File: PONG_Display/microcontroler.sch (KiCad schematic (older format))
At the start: 16 parts

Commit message: V3
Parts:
- added BT?: Battery_Cell, symbol Device:Battery_Cell
- added C? (x2): 22p, symbol Device:C
- added C? (x6): 100n, symbol Device:C
- added R? (x2): 10k, symbol Device:R
- added U?: MCP7940N-xST, symbol Timer:MCP7940N-xST
- added Y?: 32,768kHz, symbol Device:Crystal
- C?: value C -> 100n
- L?: value L -> 10u
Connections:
- net LIGHT_SENSOR_IN is gone; now on net LIGHT_SENSOR_OUT: U?.19 (ADC6)
- net +5V: now also C?.1, C?.1, R?.1, R?.1
- net GND: now also BT?.2 (-), C?.1, C?.2, C?.2, C?.2, C?.2, C?.2, C?.2, C?.2, U?.4 (VSS)
- net LIGHT_SENSOR_OUT: no longer U?.22 (ADC7)
- net PIR_SENSOR_OUT: now also U?.32 (PD2); no longer U?.13 (PB1)
- net uC_MISO: now also U?.16 (PB4)
- net uC_MOSI: now also U?.15 (PB3)
- net uC_RST: now also C?.1, D?.2 (A), R?.2, SW?.1, U?.29 (~RESET~/PC6)
- net uC_SCK: now also U?.17 (PB5)
- net ESP_RX: now reaches U?.30 (PD0)
- net ESP_TX: now reaches U?.31 (PD1)
- new net: C?.2, U?.1 (X1), Y?.1
- new net: C?.1, U?.2 (X2), Y?.2
- new net: BT?.1 (+), U?.3 (VBAT)
- new net +3V3: C?.1, C?.1, C?.1, C?.1, U?.8 (VCC)
- new net RTC_SCL: R?.2, U?.6 (SCL)
- new net RTC_SDA: R?.2, U?.5 (SDA)
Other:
- note added: "Układ RTCC"
- note added: "Złącze programowania mikrokontrolera"
- moved on the sheet: C?, D?, L?, R?, SW?, U?, Y?

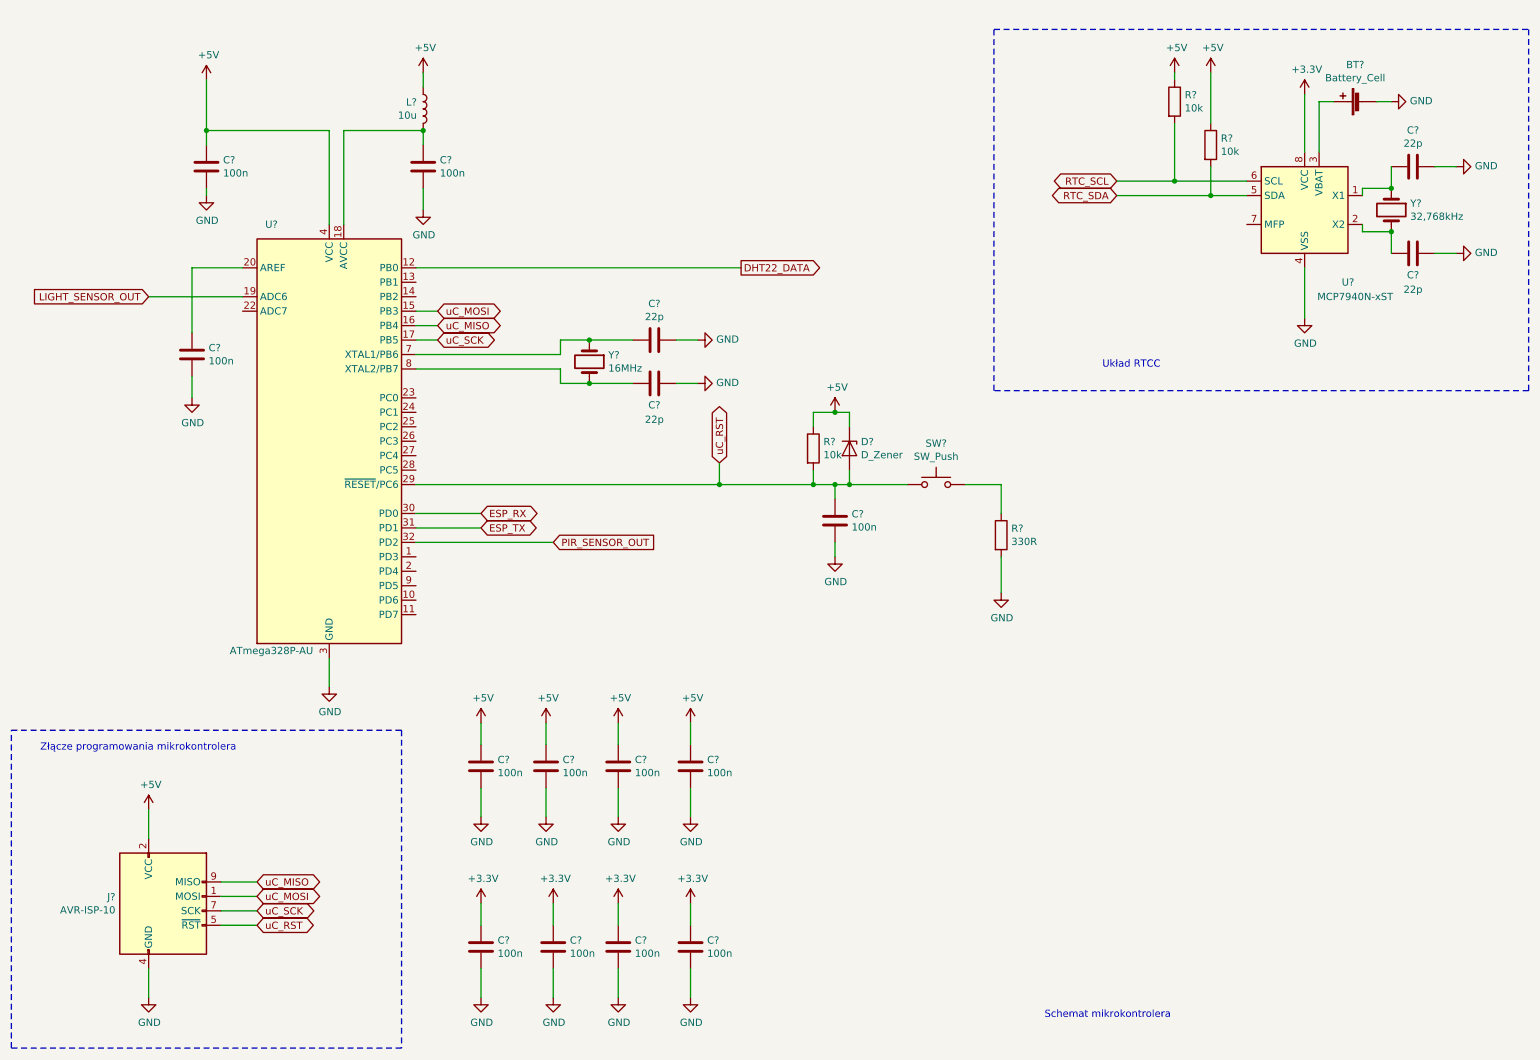
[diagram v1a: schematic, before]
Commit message: Dodane footprinty
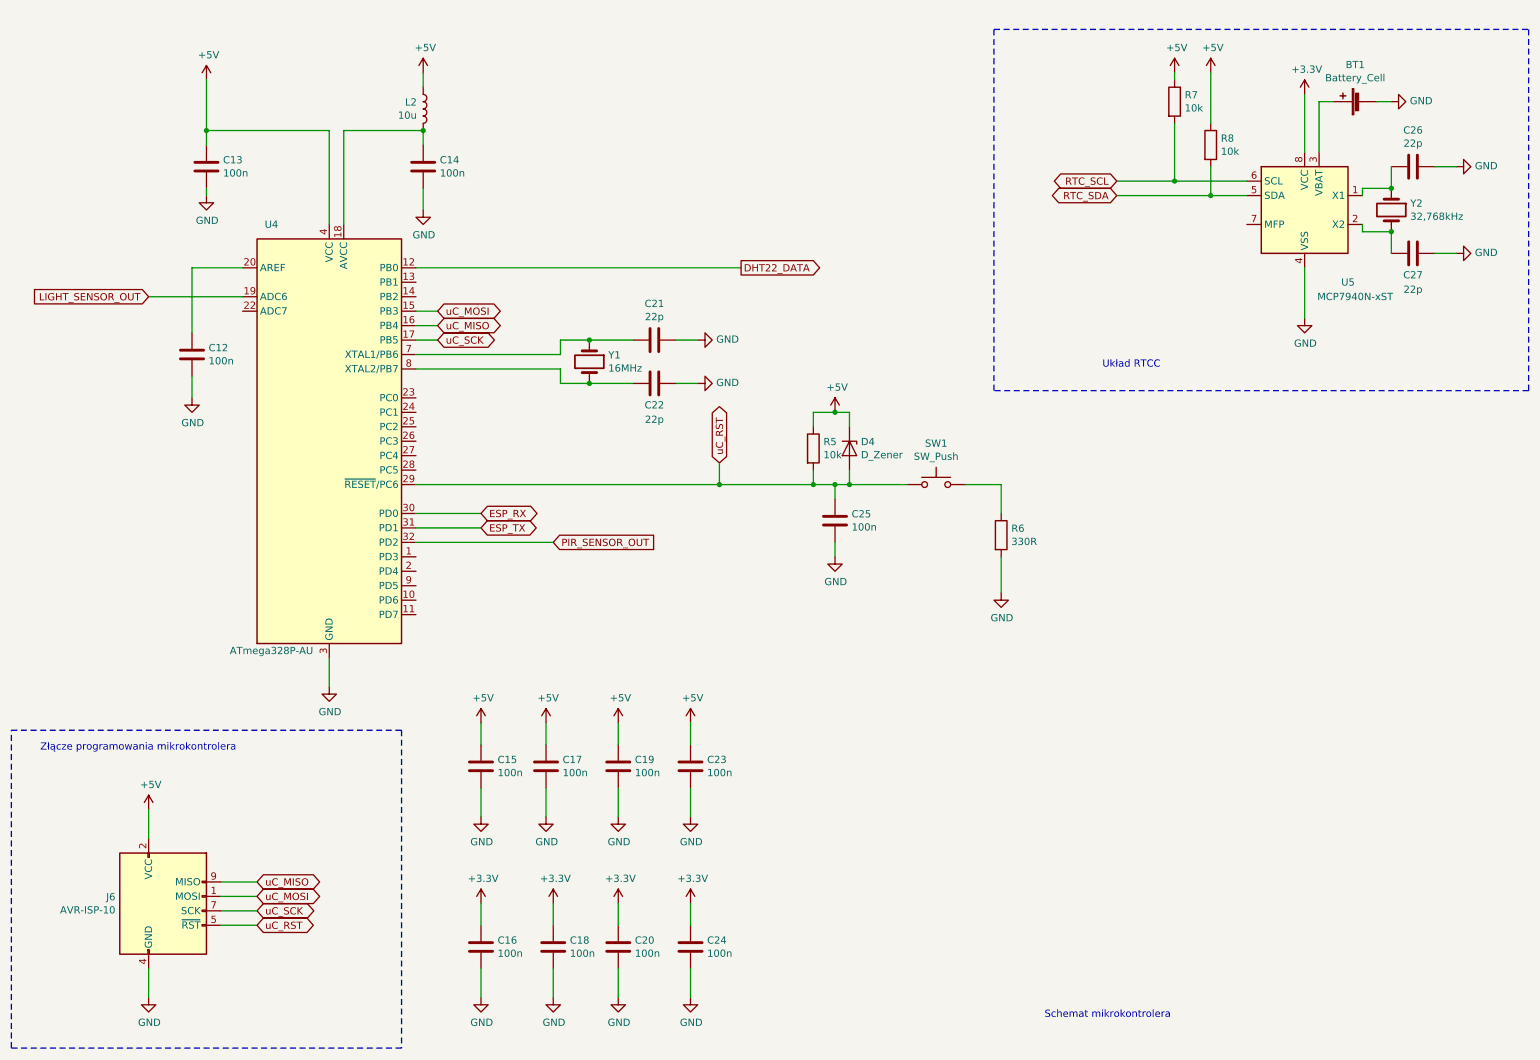
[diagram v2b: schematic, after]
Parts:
- BT1: renamed from BT?; footprint (none) -> Battery:Battery_Panasonic_CR2032-VS1N_Vertical_CircularHoles
- C12, C13, C14, C15, C16, C17, C18, C19, C20, C21, C22, C23, C24, C25, C26, C27: renamed from C?; footprint (none) -> Capacitor_SMD:C_1206_3216Metric_Pad1.42x1.75mm_HandSolder
- R5, R6, R7, R8: renamed from R?; footprint (none) -> Resistor_SMD:R_1206_3216Metric_Pad1.42x1.75mm_HandSolder
- Y1: renamed from Y?; footprint (none) -> Crystal:Crystal_HC49-4H_Vertical
- Y2: renamed from Y?; footprint (none) -> Crystal:Crystal_C38-LF_D3.0mm_L8.0mm_Horizontal
- gave numbers to parts that had none: 6

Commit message: v2
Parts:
- BT1: footprint Battery:Battery_Panasonic_CR2032-VS1N_Vertical_CircularHoles -> Battery:BatteryHolder_Keystone_1058_1x2032
- D4: footprint (none) -> Diode_THT:D_T-1_P10.16mm_Horizontal
- J6: footprint (none) -> Connector_IDC:IDC-Header_2x05_P2.54mm_Vertical
- SW1: footprint (none) -> Button_Switch_THT:SW_PUSH_6mm
- U5: footprint (none) -> Package_SO:TSSOP-8_4.4x3mm_P0.65mm
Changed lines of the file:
@@
 F 0 "J6" H 1320 6846 50  0000 R CNN
 F 1 "AVR-ISP-10" H 1320 6755 50  0000 R CNN
-F 2 "" V 1400 6800 50  0001 C CNN
+F 2 "Connector_IDC:IDC-Header_2x05_P2.54mm_Vertical" V 1400 6800 50  0001 C CNN
 F 3 " ~" H 375 6200 50  0001 C CNN
 	1    1650 6750
@@
 F 0 "D4" V 6354 3629 50  0000 L CNN
 F 1 "D_Zener" V 6445 3629 50  0000 L CNN
-F 2 "" H 6400 3550 50  0001 C CNN
+F 2 "Diode_THT:D_T-1_P10.16mm_Horizontal" H 6400 3550 50  0001 C CNN
 F 3 "~" H 6400 3550 50  0001 C CNN
 	1    6400 3550
@@
 F 0 "SW1" H 7000 4085 50  0000 C CNN
 F 1 "SW_Push" H 7000 3994 50  0000 C CNN
-F 2 "" H 7000 4000 50  0001 C CNN
+F 2 "Button_Switch_THT:SW_PUSH_6mm" H 7000 4000 50  0001 C CNN
 F 3 "~" H 7000 4000 50  0001 C CNN
 	1    7000 3800
@@
 F 0 "U5" H 9850 1400 50  0000 C CNN
 F 1 "MCP7940N-xST" H 9900 1300 50  0000 C CNN
-F 2 "" H 9550 1900 50  0001 C CNN
+F 2 "Package_SO:TSSOP-8_4.4x3mm_P0.65mm" H 9550 1900 50  0001 C CNN
 F 3 "http://ww1.microchip.com/downloads/en/DeviceDoc/20005010F.pdf" H 9550 1900 50  0001 C CNN
 	1    9550 1900
@@
 F 0 "BT1" V 10205 1200 50  0000 C CNN
 F 1 "Battery_Cell" V 10114 1200 50  0000 C CNN
-F 2 "Battery:Battery_Panasonic_CR2032-VS1N_Vertical_CircularHoles" V 9950 1210 50  0001 C CNN
+F 2 "Battery:BatteryHolder_Keystone_1058_1x2032" V 9950 1210 50  0001 C CNN
 F 3 "~" V 9950 1210 50  0001 C CNN
 	1    9950 1150

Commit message: Updated
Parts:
- added RV?: R_POT, Potentiometer_THT:Potentiometer_Piher_PT-6-V_Vertical, symbol Device:R_POT
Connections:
- net GND: now also RV?.3
- net LIGHT_SENSOR_OUT: now also RV?.1; no longer U4.19 (ADC6)
- new net: RV?.2, U4.19 (ADC6)
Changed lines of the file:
@@
 Wire Wire Line
 	5200 3100 5350 3100
-Text GLabel 1550 2500 0    50   Input ~ 0
+Text GLabel 1100 1900 1    50   Input ~ 0
 LIGHT_SENSOR_OUT
-Wire Wire Line
-	1550 2500 2200 2500
 $Comp
 L power:+5V #PWR0142
@@
 	1    0    0    -1
 $EndComp
+$Comp
+L Device:R_POT RV?
+U 1 1 5E88F324
+P 1100 2500
+F 0 "RV?" H 1030 2454 50  0000 R CNN
+F 1 "R_POT" H 1030 2545 50  0000 R CNN
+F 2 "Potentiometer_THT:Potentiometer_Piher_PT-6-V_Vertical" H 1100 2500 50  0001 C CNN
+F 3 "~" H 1100 2500 50  0001 C CNN
+	1    1100 2500
+	1    0    0    -1
+$EndComp
+$Comp
+L power:GND #PWR?
+U 1 1 5E88F32A
+P 1150 2850
+F 0 "#PWR?" H 1150 2600 50  0001 C CNN
+F 1 "GND" H 1155 2677 50  0000 C CNN
+F 2 "" H 1150 2850 50  0001 C CNN
+F 3 "" H 1150 2850 50  0001 C CNN
+	1    1150 2850
+	0    -1   -1   0
+$EndComp
+Wire Wire Line
+	1150 2850 1100 2850
+Wire Wire Line
+	1100 2850 1100 2650
+Wire Wire Line
+	1100 2350 1100 1900
+Wire Wire Line
+	1250 2500 2200 2500
 $EndSCHEMATC

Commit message: napisałem coś
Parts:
- J6: symbol Connector:AVR-ISP-10 -> PONG_Display-rescue:AVR-ISP-10-Connector
- U4: symbol MCU_Microchip_ATmega:ATmega328P-AU -> PONG_Display-rescue:ATmega328P-AU-MCU_Microchip_ATmega
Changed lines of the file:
@@
 EESchema Schematic File Version 4
+LIBS:PONG_Display-cache
 EELAYER 30 0
 EELAYER END
@@
 $EndDescr
 $Comp
-L Connector:AVR-ISP-10 J?
+L PONG_Display-rescue:AVR-ISP-10-Connector J?
 U 1 1 5E830B15
 P 1650 6750
 AR Path="/5E80CCDD/5E830B15" Ref="J?"  Part="1"
 AR Path="/5E80B18F/5E830B15" Ref="J6"  Part="1"
+AR Path="/5E830B15" Ref="J6"  Part="1"
 F 0 "J6" H 1320 6846 50  0000 R CNN
 F 1 "AVR-ISP-10" H 1320 6755 50  0000 R CNN
@@
 Schemat mikrokontrolera
 $Comp
-L MCU_Microchip_ATmega:ATmega328P-AU U4
+L PONG_Display-rescue:ATmega328P-AU-MCU_Microchip_ATmega U4
 U 1 1 5E85008B
 P 2800 3500
